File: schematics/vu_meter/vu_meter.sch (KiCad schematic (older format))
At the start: 49 parts, among them U10 LM339, U14 LM833N, U8 LM339, U9 LM339

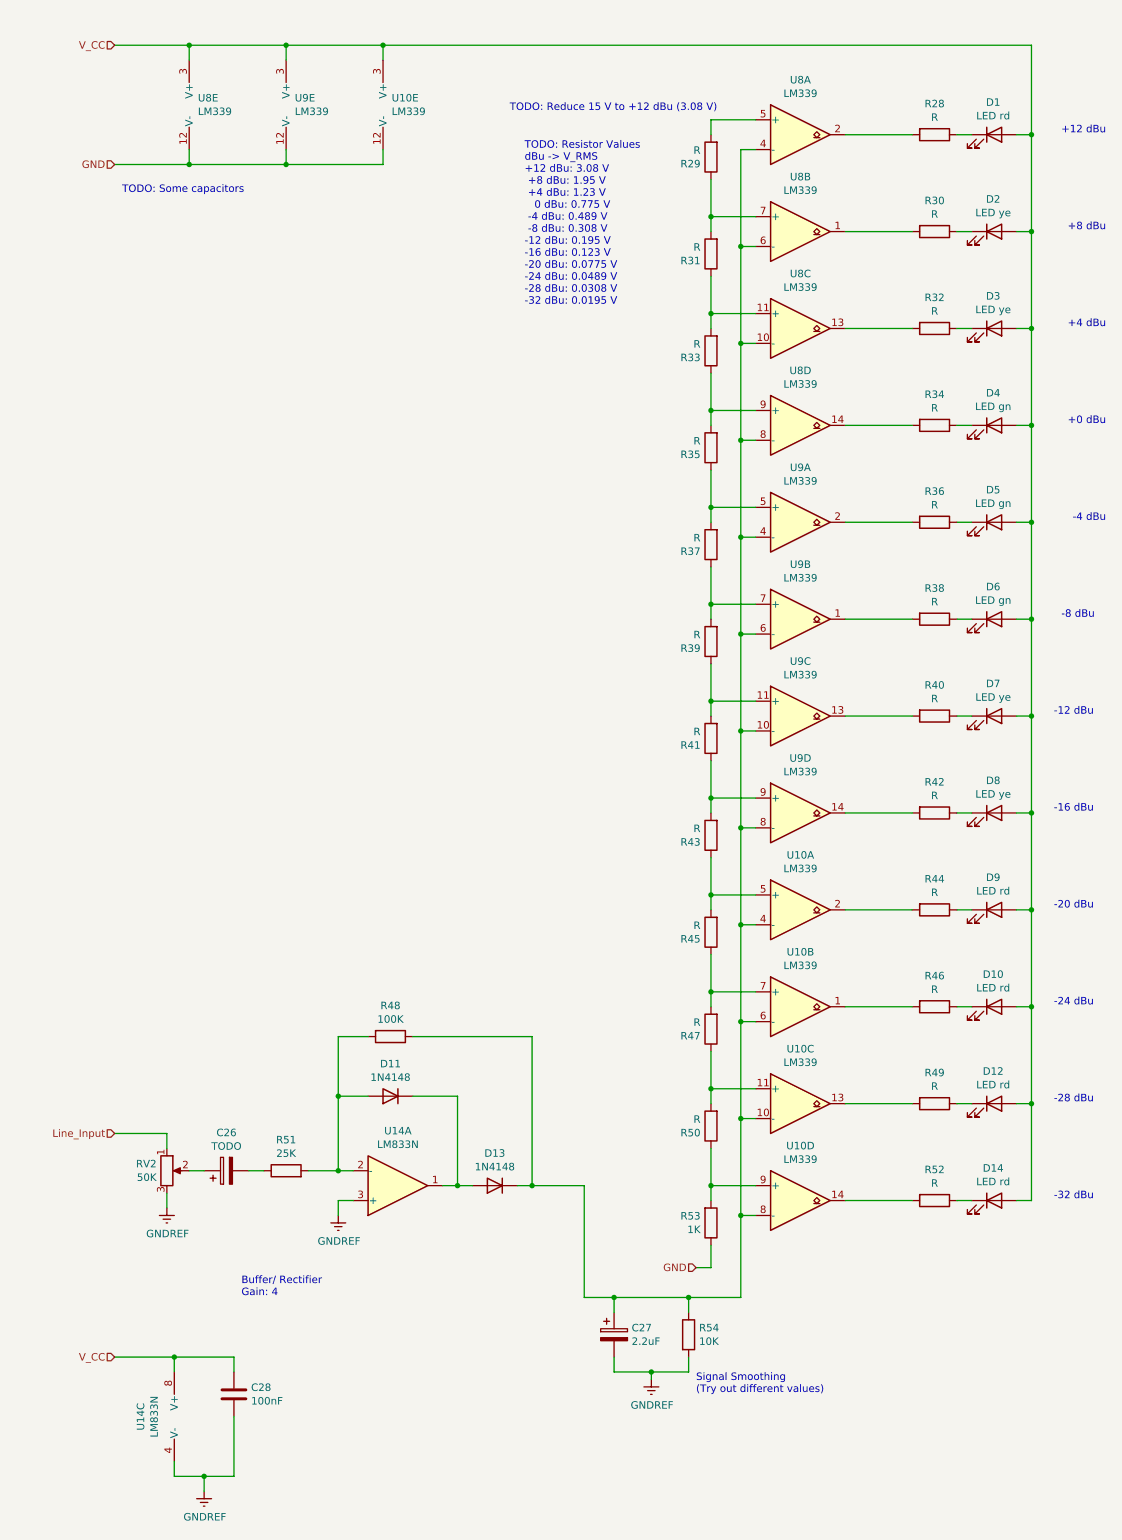
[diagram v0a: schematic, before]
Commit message: Move VU-Meter to own project
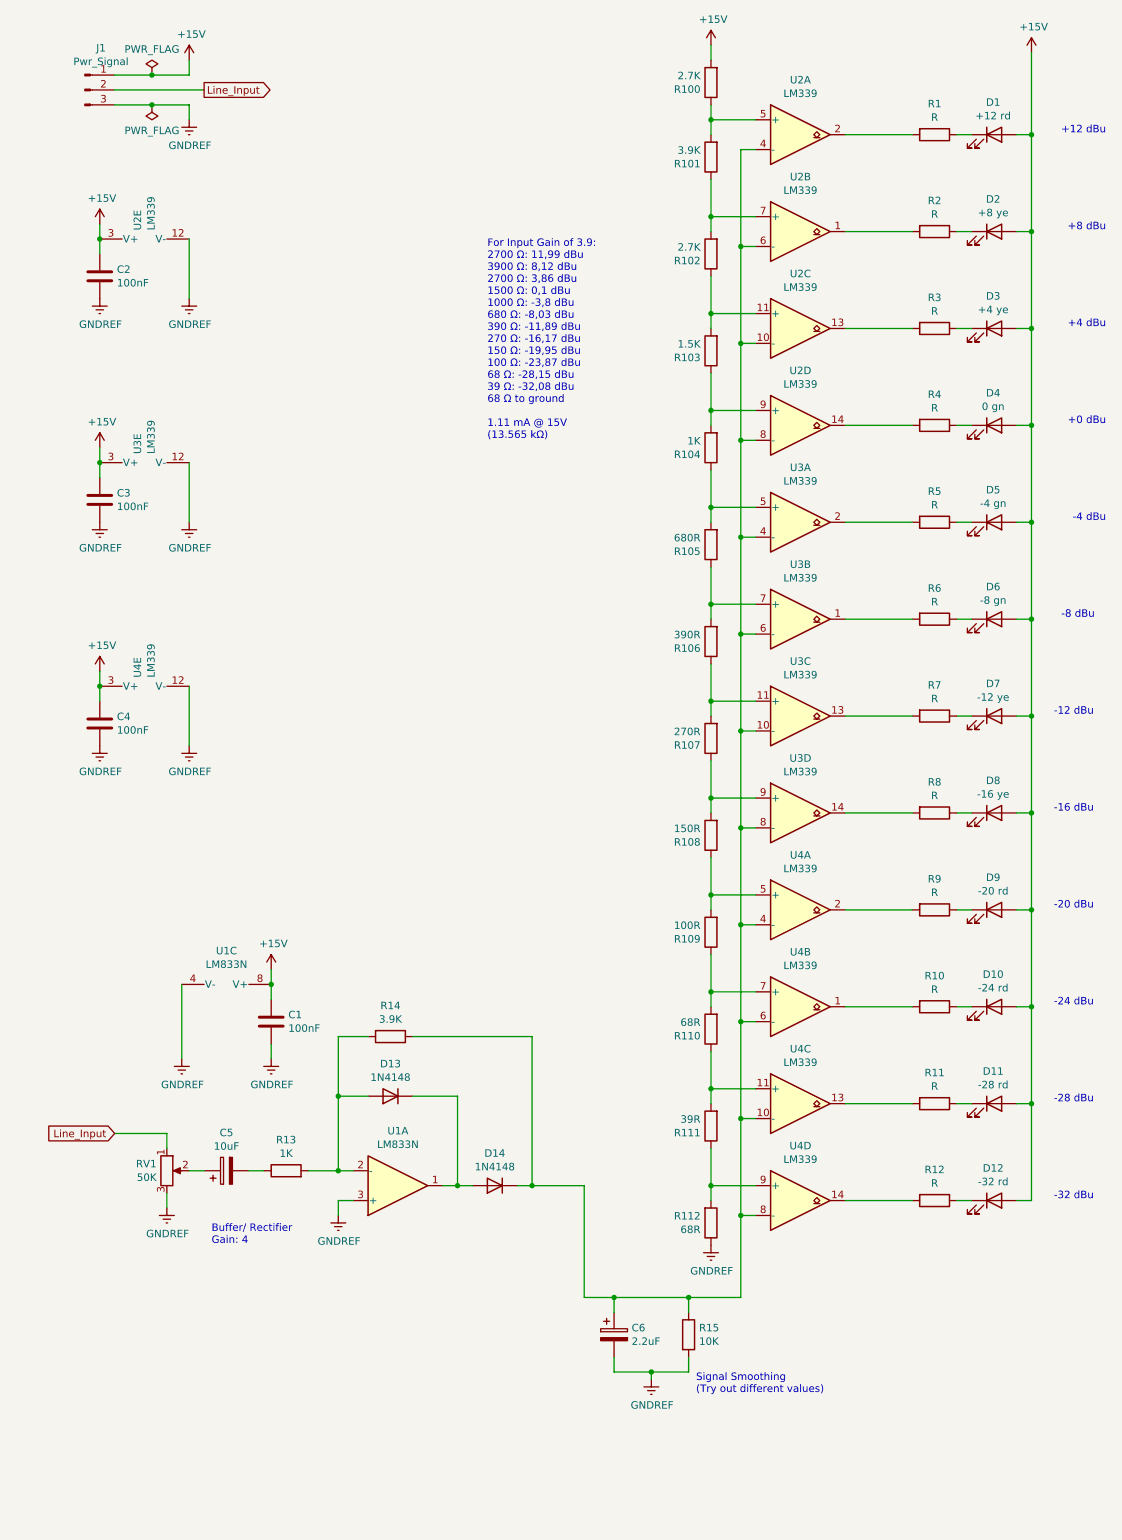
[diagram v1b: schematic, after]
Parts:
- added C2, C3, C4: 100nF, Capacitor_THT:C_Disc_D5.0mm_W2.5mm_P2.50mm, symbol Device:C
- added J1: Pwr_Signal, Connector_PinHeader_2.54mm:PinHeader_1x03_P2.54mm_Vertical, symbol Connector:Conn_01x03_Male
- added R100: 2.7K, Resistor_THT:R_Axial_DIN0207_L6.3mm_D2.5mm_P10.16mm_Horizontal, symbol Device:R
- C5: renamed from C26; value TODO -> 10uF
- D1: value LED rd -> +12 rd
- D10: value LED rd -> -24 rd
- D11: renamed from D12; value LED rd -> -28 rd
- D12: renamed from D14; value LED rd -> -32 rd
- D2: value LED ye -> +8 ye
- D3: value LED ye -> +4 ye
- D4: value LED gn -> 0 gn
- D5: value LED gn -> -4 gn
- D6: value LED gn -> -8 gn
- D7: value LED ye -> -12 ye
- D8: value LED ye -> -16 ye
- D9: value LED rd -> -20 rd
- R101: renamed from R29; value R -> 3.9K
- R102: renamed from R31; value R -> 2.7K
- R103: renamed from R33; value R -> 1.5K
- R104: renamed from R35; value R -> 1K
- R105: renamed from R37; value R -> 680R
- R106: renamed from R39; value R -> 390R
- R107: renamed from R41; value R -> 270R
- R108: renamed from R43; value R -> 150R
- R109: renamed from R45; value R -> 100R
- R110: renamed from R47; value R -> 68R
- R111: renamed from R50; value R -> 39R
- R112: renamed from R53; value 1K -> 68R
- R13: renamed from R51; value 25K -> 1K
- R14: renamed from R48; value 100K -> 3.9K
- renumbered C28 to C1, C27 to C6, D11 to D13, D13 to D14, R28 to R1, R46 to R10, R49 to R11, R52 to R12, R54 to R15, R30 to R2, R32 to R3, R34 to R4, R36 to R5, R38 to R6, R40 to R7, R42 to R8, R44 to R9, RV2 to RV1, U14 to U1, U8 to U2, U9 to U3, U10 to U4
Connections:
- net GND is gone; now on net GNDREF: R112.1, U2.12 (V-), U3.12 (V-), U4.12 (V-)
- net GNDREF: now also C2.2, C3.2, C4.2, J1.3 (Pin_3)
- net Line_Input: now also J1.2 (Pin_2)
- net at R101.2, U2.5 (+): now also R100.1
- net V_CC renamed +15V
- net +15V: now also C2.1, C3.1, C4.1, J1.1 (Pin_1), R100.2
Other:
- note added: "For Input Gain of 3.9:\n2700 Ω: 11,99 dBu\n3900 Ω: 8,12 dBu\n2700 Ω: 3,86 dBu\n1500 Ω: 0,1 dBu\n1000 Ω: -3,8 dBu\n680 Ω: -8,03 dBu\n390 Ω: -11,89 dBu\n270 Ω: -16,17 dBu\n150 Ω: -19,95 dBu\n100 Ω: -23,87 dBu\n68 Ω: -28,15 dBu\n39 Ω: -32,08 dBu\n68 Ω to ground\n\n1.11 mA @ 15V\n(13.565 kΩ)"
- note removed: "TODO: Reduce 15 V to +12 dBu (3.08 V)"
- note removed: "TODO: Resistor Values\ndBu -> V_RMS\n+12 dBu: 3.08 V\n +8 dBu: 1.95 V\n +4 dBu: 1.23 V\n 0 dBu: 0.775 V\n -4 dBu: 0.489 V\n -8 dBu: 0.308 V\n-12 dBu: 0.195 V\n-16 dBu: 0.123 V\n-20 dBu: 0.0775 V\n-24 dBu: 0.0489 V\n-28 dBu: 0.0308 V\n-32 dBu: 0.0195 V"
- note removed: "TODO: Some capacitors"
- moved on the sheet: C1, U1C, U2E, U3E, U4E

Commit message: final fixes for first prototype PCB order
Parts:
- C5: footprint Capacitor_THT:CP_Radial_D10.0mm_P5.00mm -> Capacitor_THT:CP_Radial_D5.0mm_P2.50mm
- C6: footprint Capacitor_THT:CP_Radial_D10.0mm_P5.00mm -> Capacitor_THT:CP_Radial_D10.0mm_P2.50mm_P5.00mm
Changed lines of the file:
@@
 Sheet 1 1
 Title "VU Meter Module"
-Date "2020-11-08"
+Date "2020-11-12"
 Rev "v0.1"
 Comp "Jannik Beyerstedt"
@@
 F 0 "C6" H 4468 9396 50  0000 L CNN
 F 1 "2.2uF" H 4468 9305 50  0000 L CNN
-F 2 "Capacitor_THT:CP_Radial_D10.0mm_P5.00mm" H 4388 9200 50  0001 C CNN
+F 2 "Capacitor_THT:CP_Radial_D10.0mm_P2.50mm_P5.00mm" H 4388 9200 50  0001 C CNN
 F 3 "~" H 4350 9350 50  0001 C CNN
 	1    4350 9350
@@
 F 0 "C5" V 2005 8250 50  0000 C CNN
 F 1 "10uF" V 1914 8250 50  0000 C CNN
-F 2 "Capacitor_THT:CP_Radial_D10.0mm_P5.00mm" H 1788 8100 50  0001 C CNN
+F 2 "Capacitor_THT:CP_Radial_D5.0mm_P2.50mm" H 1788 8100 50  0001 C CNN
 F 3 "~" H 1750 8250 50  0001 C CNN
 	1    1750 8250

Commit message: VU meter: add -15V, fix footprints, specify LED resistors
TODO: Decide on signal smoothing
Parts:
- added C7: 100nF, Capacitor_THT:C_Disc_D5.0mm_W2.5mm_P5.00mm, symbol Device:C
- added H1, H2, H3, H4: MountingHole, MountingHole:MountingHole_3.2mm_M3_ISO14580, symbol Mechanical:MountingHole
- C1, C2, C3, C4: footprint Capacitor_THT:C_Disc_D5.0mm_W2.5mm_P2.50mm -> Capacitor_THT:C_Disc_D5.0mm_W2.5mm_P5.00mm
- C5: value 10uF -> 1uF
- C6: value 2.2uF -> 47uF
- D1, D10, D11, D12, D9: Model (none) -> TLHR5405
- D2, D3, D7, D8: Model (none) -> TLHY5405
- D4, D5, D6: Model (none) -> TLHG5405
- J1: footprint Connector_PinHeader_2.54mm:PinHeader_1x03_P2.54mm_Vertical -> Connector_PinHeader_2.54mm:PinHeader_1x04_P2.54mm_Vertical; symbol Connector:Conn_01x03_Male -> Connector:Conn_01x04_Male; Model (none) -> TODO: Actual Connector
- R1, R10, R11, R12, R2, R3, R4, R5, R6, R7, R8, R9: value R -> 390R
- R15: value 10K -> 100K
- RV1: footprint Potentiometer_THT:Potentiometer_Vishay_148-149_Single_Horizontal -> Potentiometer_THT:Potentiometer_Vishay_T73XX_Horizontal; Model (none) -> Vishay M64{Y,Z}503K
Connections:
- net +15V: now also J1.3 (Pin_3); no longer J1.1 (Pin_1)
- net GNDREF: now also J1.1 (Pin_1), C7.1; no longer J1.3 (Pin_3), U1.4 (V-)
- net Line_Input: now also J1.4 (Pin_4); no longer J1.2 (Pin_2)
- new net -15V: C7.2, J1.2 (Pin_2), U1.4 (V-)
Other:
- note added: "Buffer/ Rectifier\nGain: 3.9"
- note added: "Signal Smoothing\nTODO: Remove all together!?"
- note added: "TODO: Better use 5V?\nrd: 2.3 V (390R @15V)\ngn: 2.4 V (390R @15V)\nye: 2.6 V (390R @15V)"
- note removed: "Buffer/ Rectifier\nGain: 4"
- note removed: "Signal Smoothing\n(Try out different values)"

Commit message: Main: Add 15V phantom power
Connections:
- net labels added: GND
- net labels removed: GNDREF
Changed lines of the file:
@@
 $EndComp
 $Comp
-L power:GNDREF #PWR017
+L power:GND #PWR017
 U 1 1 5FD55EE5
 P 4600 9650
@@
 AR Path="/5FA7BAE6/5FD55EE5" Ref="#PWR041"  Part="1"
 F 0 "#PWR017" H 4600 9400 50  0001 C CNN
-F 1 "GNDREF" H 4605 9477 50  0000 C CNN
+F 1 "GND" H 4605 9477 50  0000 C CNN
 F 2 "" H 4600 9650 50  0001 C CNN
 F 3 "" H 4600 9650 50  0001 C CNN
@@
 $EndComp
 $Comp
-L power:GNDREF #PWR018
+L power:GND #PWR018
 U 1 1 5FCB34D1
 P 1450 7500
@@
 AR Path="/5FA7BAE6/5FCB34D1" Ref="#PWR042"  Part="1"
 F 0 "#PWR018" H 1450 7250 50  0001 C CNN
-F 1 "GNDREF" H 1455 7327 50  0000 C CNN
+F 1 "GND" H 1455 7327 50  0000 C CNN
 F 2 "" H 1450 7500 50  0001 C CNN
 F 3 "" H 1450 7500 50  0001 C CNN
@@
 	3200 8350 3300 8350
 $Comp
-L power:GNDREF #PWR015
+L power:GND #PWR015
 U 1 1 5FCB351D
 P 2500 8550
@@
 AR Path="/5FA7BAE6/5FCB351D" Ref="#PWR040"  Part="1"
 F 0 "#PWR015" H 2500 8300 50  0001 C CNN
-F 1 "GNDREF" H 2505 8377 50  0000 C CNN
+F 1 "GND" H 2505 8377 50  0000 C CNN
 F 2 "" H 2500 8550 50  0001 C CNN
 F 3 "" H 2500 8550 50  0001 C CNN
@@
 	1500 8250 1600 8250
 $Comp
-L power:GNDREF #PWR014
+L power:GND #PWR014
 U 1 1 5FFA8E8D
 P 1350 8500
@@
 AR Path="/5FA7BAE6/5FFA8E8D" Ref="#PWR039"  Part="1"
 F 0 "#PWR014" H 1350 8250 50  0001 C CNN
-F 1 "GNDREF" H 1355 8327 50  0000 C CNN
+F 1 "GND" H 1355 8327 50  0000 C CNN
 F 2 "" H 1350 8500 50  0001 C CNN
 F 3 "" H 1350 8500 50  0001 C CNN
@@
 $EndComp
 $Comp
-L power:GNDREF #PWR06
+L power:GND #PWR06
 U 1 1 5FB1F99A
 P 900 2400
 F 0 "#PWR06" H 900 2150 50  0001 C CNN
-F 1 "GNDREF" H 905 2227 50  0000 C CNN
+F 1 "GND" H 905 2227 50  0000 C CNN
 F 2 "" H 900 2400 50  0001 C CNN
 F 3 "" H 900 2400 50  0001 C CNN
@@
 Connection ~ 7150 1300
 $Comp
-L power:GNDREF #PWR07
+L power:GND #PWR07
 U 1 1 5FB7DBA4
 P 1500 2400
 F 0 "#PWR07" H 1500 2150 50  0001 C CNN
-F 1 "GNDREF" H 1505 2227 50  0000 C CNN
+F 1 "GND" H 1505 2227 50  0000 C CNN
 F 2 "" H 1500 2400 50  0001 C CNN
 F 3 "" H 1500 2400 50  0001 C CNN
@@
 $EndComp
 $Comp
-L power:GNDREF #PWR08
+L power:GND #PWR08
 U 1 1 5FBCBBA0
 P 900 3900
 F 0 "#PWR08" H 900 3650 50  0001 C CNN
-F 1 "GNDREF" H 905 3727 50  0000 C CNN
+F 1 "GND" H 905 3727 50  0000 C CNN
 F 2 "" H 900 3900 50  0001 C CNN
 F 3 "" H 900 3900 50  0001 C CNN
@@
 $EndComp
 $Comp
-L power:GNDREF #PWR09
+L power:GND #PWR09
 U 1 1 5FBCBBA6
 P 1500 3900
 F 0 "#PWR09" H 1500 3650 50  0001 C CNN
-F 1 "GNDREF" H 1505 3727 50  0000 C CNN
+F 1 "GND" H 1505 3727 50  0000 C CNN
 F 2 "" H 1500 3900 50  0001 C CNN
 F 3 "" H 1500 3900 50  0001 C CNN
@@
 $EndComp
 $Comp
-L power:GNDREF #PWR010
+L power:GND #PWR010
 U 1 1 5FC56406
 P 900 5400
 F 0 "#PWR010" H 900 5150 50  0001 C CNN
-F 1 "GNDREF" H 905 5227 50  0000 C CNN
+F 1 "GND" H 905 5227 50  0000 C CNN
 F 2 "" H 900 5400 50  0001 C CNN
 F 3 "" H 900 5400 50  0001 C CNN
@@
 $EndComp
 $Comp
-L power:GNDREF #PWR011
+L power:GND #PWR011
 U 1 1 5FC5640C
 P 1500 5400
 F 0 "#PWR011" H 1500 5150 50  0001 C CNN
-F 1 "GNDREF" H 1505 5227 50  0000 C CNN
+F 1 "GND" H 1505 5227 50  0000 C CNN
 F 2 "" H 1500 5400 50  0001 C CNN
 F 3 "" H 1500 5400 50  0001 C CNN
@@
 Connection ~ 900  3500
 $Comp
-L power:GNDREF #PWR0101
+L power:GND #PWR0101
 U 1 1 5FCA9B50
 P 5000 8750
@@
 AR Path="/5FA7BAE6/5FCA9B50" Ref="#PWR?"  Part="1"
 F 0 "#PWR0101" H 5000 8500 50  0001 C CNN
-F 1 "GNDREF" H 5005 8577 50  0000 C CNN
+F 1 "GND" H 5005 8577 50  0000 C CNN
 F 2 "" H 5000 8750 50  0001 C CNN
 F 3 "" H 5000 8750 50  0001 C CNN
@@
 $EndComp
 $Comp
-L power:GNDREF #PWR0102
+L power:GND #PWR0102
 U 1 1 5FCEE917
 P 2050 7500
@@
 AR Path="/5FA7BAE6/5FCEE917" Ref="#PWR?"  Part="1"
 F 0 "#PWR0102" H 2050 7250 50  0001 C CNN
-F 1 "GNDREF" H 2055 7327 50  0000 C CNN
+F 1 "GND" H 2055 7327 50  0000 C CNN
 F 2 "" H 2050 7500 50  0001 C CNN
 F 3 "" H 2050 7500 50  0001 C CNN
@@
 TODO: Better use 5V?\nrd: 2.3 V (390R @15V)\ngn: 2.4 V (390R @15V)\nye: 2.6 V (390R @15V)
 $Comp
-L power:GNDREF #PWR013
+L power:GND #PWR013
 U 1 1 5FABEB24
 P 1600 1200
 F 0 "#PWR013" H 1600 950 50  0001 C CNN
-F 1 "GNDREF" H 1605 1027 50  0000 C CNN
+F 1 "GND" H 1605 1027 50  0000 C CNN
 F 2 "" H 1600 1200 50  0001 C CNN
 F 3 "" H 1600 1200 50  0001 C CNN
